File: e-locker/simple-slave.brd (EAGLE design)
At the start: 88.1 x 80 mm, 43 parts, among them Q1 16MHz, U1 ATMEGA328, U2 MAX487ESA+TCBX, X1 JST-XH-02-PIN-LONG-PAD, X10 JST-XH-04-PIN-LONG-PAD, X11 JST-XH-02-PIN-LONG-PAD, X2 JST-XH-05-PIN-LONG-PAD, X3 JST-XH-04-PIN-LONG-PAD, X4 JST-XH-04-PIN-LONG-PAD, X5 JST-XH-04-PIN-LONG-PAD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

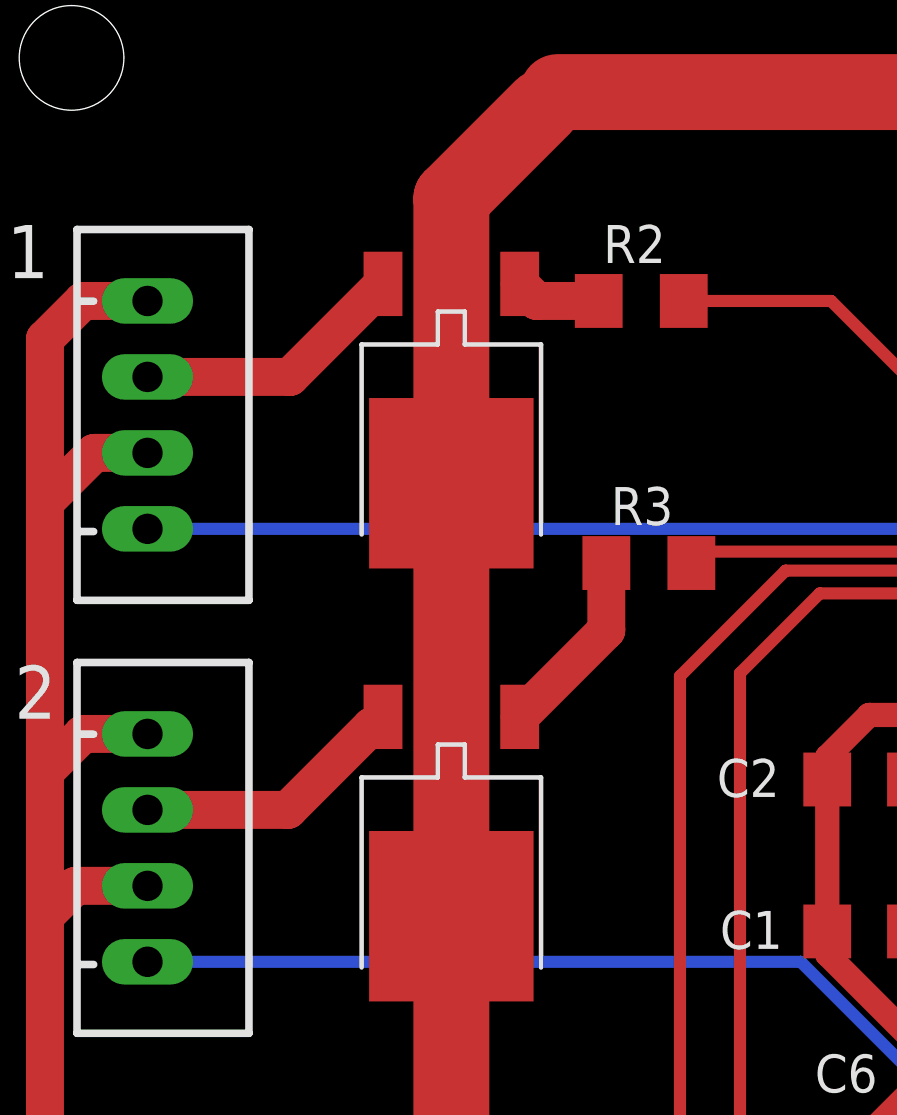
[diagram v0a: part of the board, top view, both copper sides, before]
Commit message: incorrect mosfets - WIP
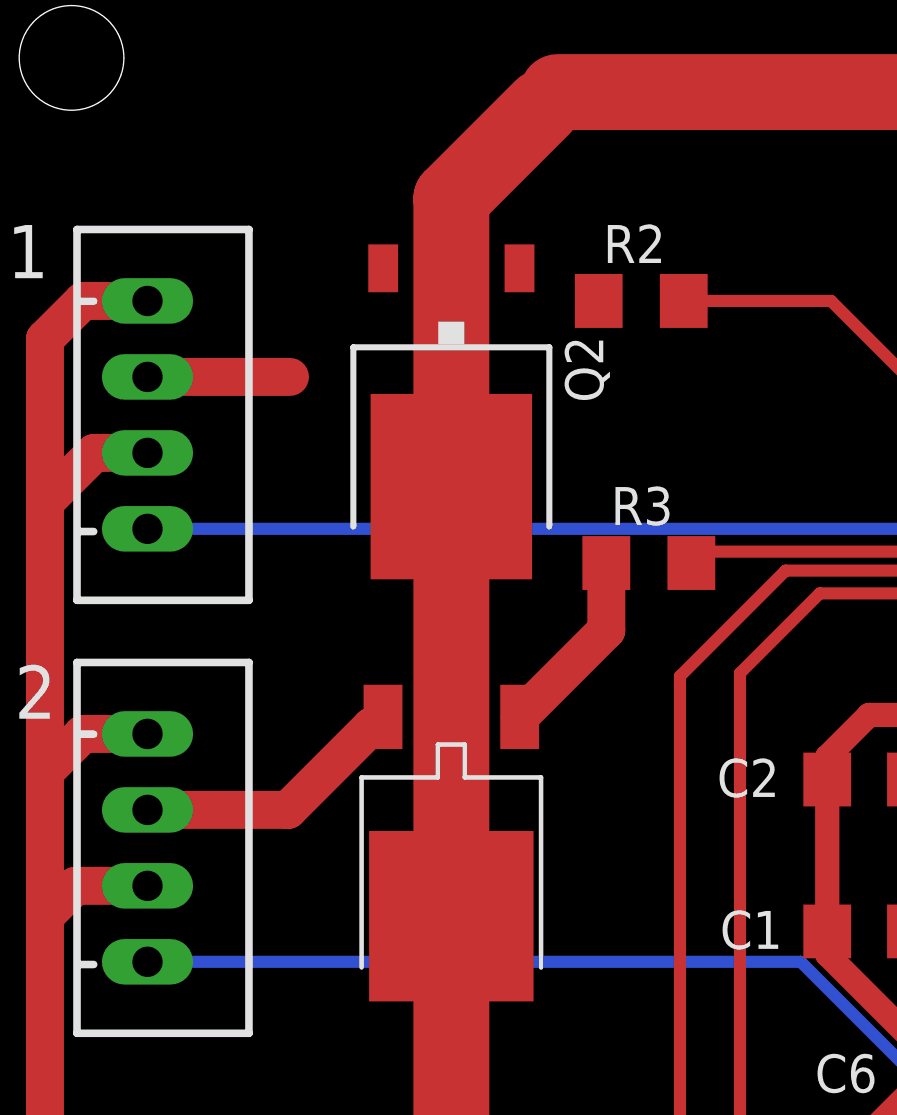
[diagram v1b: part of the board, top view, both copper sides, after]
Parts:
- removed U$1: (no value), dawidkulpa_dev:TO252
- added Q2: SPD30P06PTO252, transistor-fet:TO252
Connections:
- net N$1: now also Q2.1; no longer U$1.P1
- net N$11: now also Q2.3; no longer U$1.P3
- net V24: now also Q2.2; no longer U$1.P2
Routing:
- net V24: track 318.4 -> 294.1 mm
- net N$11: track 9.16 -> 4.77 mm
- net N$1: track 2.88 -> 0.00 mm
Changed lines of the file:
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@@
 <?xml version="1.0" encoding="utf-8"?>
 <!DOCTYPE eagle SYSTEM "eagle.dtd">
-<eagle version="9.2.2">
+<eagle version="9.6.2">
 <drawing>
 <settings>
@@
 <attribute name="VALUE" x="66.802" y="63.754" size="1.27" layer="27" rot="R180"/>
 </element>
-<element name="U$1" library="dawidkulpa_dev" package="TO252" value="" x="16.51" y="64.262" smashed="yes" rot="R180"/>
 <element name="U$2" library="dawidkulpa_dev" package="TO252" value="" x="16.51" y="49.784" smashed="yes" rot="R180"/>
 <element name="U$3" library="dawidkulpa_dev" package="TO252" value="" x="16.383" y="33.401" smashed="yes" rot="R180"/>
@@
 </element>
 <element name="U$9" library="zort-library" package="ELOCKER" value="" x="60.6044" y="2.1844" smashed="yes"/>
+<element name="Q2" library="transistor-fet" library_urn="urn:adsk.eagle:library:396" package="TO252" package3d_urn="urn:adsk.eagle:package:28537/2" value="SPD30P06PTO252" x="16.51" y="64.3636" smashed="yes" rot="R180">
+<attribute name="NAME" x="20.32" y="66.9036" size="1.27" layer="25" rot="R270"/>
+<attribute name="POPULARITY" value="3" x="16.51" y="64.3636" size="1.778" layer="27" rot="R180" display="off"/>
+<attribute name="VALUE" x="11.43" y="66.9036" size="1.27" layer="27" rot="R270"/>
+</element>
 </elements>
 <signals>
@@
 <contactref element="C8" pad="1"/>
 <contactref element="C4" pad="+"/>
-<contactref element="U$1" pad="P2"/>
 <contactref element="U$2" pad="P2"/>
 <contactref element="U$3" pad="P2"/>
@@
 <contactref element="U$8" pad="P2"/>
 <wire x1="22.352" y1="11.3928" x2="22.264" y2="11.4808" width="1.27" layer="1"/>
-<wire x1="16.765" y1="61.722" x2="16.51" y2="61.977" width="1.27" layer="1"/>
-<wire x1="16.51" y1="61.977" x2="16.51" y2="47.499" width="1.27" layer="1"/>
 <wire x1="16.51" y1="47.499" x2="16.51" y2="31.243" width="1.27" layer="1"/>
 <wire x1="16.51" y1="31.243" x2="16.383" y2="31.116" width="1.27" layer="1"/>
@@
 <wire x1="71.882" y1="33.782" x2="72.263" y2="33.782" width="1.27" layer="1"/>
 <wire x1="72.263" y1="18.923" x2="72.136" y2="18.923" width="1.27" layer="1"/>
-<wire x1="16.51" y1="71.501" x2="16.51" y2="61.977" width="1.27" layer="1"/>
 <wire x1="20.066" y1="75.057" x2="62.103" y2="75.057" width="1.27" layer="1"/>
 <wire x1="20.066" y1="75.057" x2="19.558" y2="74.549" width="1.27" layer="1"/>
@@
 <wire x1="71.882" y1="50.926" x2="71.882" y2="67.309" width="2.54" layer="1"/>
 <wire x1="16.51" y1="71.501" x2="16.51" y2="14.606" width="2.54" layer="1"/>
+<contactref element="Q2" pad="2"/>
 <wire x1="71.882" y1="50.926" x2="83.693" y2="50.799" width="0" layer="19" extent="1-1"/>
-</signal>
-<signal name="N$1">
-<contactref element="U$1" pad="P1"/>
-<contactref element="R2" pad="1"/>
-<wire x1="21.438" y1="68.072" x2="19.365" y2="68.072" width="1.27" layer="1"/>
-<wire x1="19.365" y1="68.072" x2="18.795" y2="68.642" width="1.27" layer="1"/>
+<wire x1="14.23" y1="69.1636" x2="16.51" y2="14.606" width="0" layer="19" extent="1-1"/>
 </signal>
 <signal name="N$2">
@@
 <signal name="N$11">
 <contactref element="X3" pad="2"/>
-<contactref element="U$1" pad="P3"/>
 <wire x1="6.35" y1="65.532" x2="11.115" y2="65.532" width="1.27" layer="1"/>
-<wire x1="11.115" y1="65.532" x2="14.225" y2="68.642" width="1.27" layer="1"/>
+<contactref element="Q2" pad="3"/>
+<wire x1="16.51" y1="61.8636" x2="6.35" y2="65.532" width="0" layer="19" extent="1-1"/>
 </signal>
 <signal name="N$12">
@@
 <wire x1="74.167" y1="60.644" x2="77.277" y2="63.754" width="1.27" layer="1"/>
 </signal>
+<signal name="N$1">
+<contactref element="R2" pad="1"/>
+<contactref element="Q2" pad="1"/>
+<wire x1="18.79" y1="69.1636" x2="21.438" y2="68.072" width="0" layer="19" extent="1-1"/>
+</signal>
 </signals>
